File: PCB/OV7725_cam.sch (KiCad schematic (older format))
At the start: 0 parts

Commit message: Camera
Camera sensor and lens mount added to schematic sheet, full scheamtic to
follow
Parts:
- added LENS?: OV7725_20mm_Lens, PCB_Footprints:OV07725_20mm_Lense_Mount, symbol OV7725_20mm_Lens
- added U?: OV7725, PCB_Footprints:OV07725-V28A, symbol OV7725
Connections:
- net labels added: +1V35, +1V8, +3.3V, GND
- wire segments 0 -> 1
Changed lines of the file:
@@
 Comment4 ""
 $EndDescr
+$Comp
+L OV7725 U?
+U 1 1 5882D650
+P 4825 3375
+F 0 "U?" H 4475 4475 60  0000 C CNN
+F 1 "OV7725" H 4575 2675 60  0000 C CNN
+F 2 "PCB_Footprints:OV07725-V28A" H 4875 4575 60  0001 C CNN
+F 3 "https://cdn.shopify.com/s/files/1/0803/9211/files/OV7725.pdf?3787874186050138641" H 4975 4675 60  0001 C CNN
+F 4 "$4.379 @ 36" H 5075 4775 60  0001 C CNN "Cost"
+F 5 "8 Jan 2017" H 5175 4875 60  0001 C CNN "Date Created"
+F 6 "8 Jan 2017" H 5275 4975 60  0001 C CNN "Date Modifed"
+F 7 "Adam Vadala-Roth" H 5375 5075 60  0001 C CNN "Designer"
+F 8 "2.70mm" H 5475 5175 60  0001 C CNN "Height"
+F 9 "Yes" H 5575 5275 60  0001 C CNN "RHoS?"
+F 10 "OmniVision Technologies Inc" H 5675 5375 60  0001 C CNN "MFR"
+F 11 "OV07725-V28A" H 5775 5475 60  0001 C CNN "MFR#"
+F 12 "SMT/SMD" H 5875 5575 60  0001 C CNN "Mounting"
+F 13 "2" H 5975 5675 60  0001 C CNN "Pin Count#"
+F 14 "Active" H 6075 5775 60  0001 C CNN "Status"
+F 15 "N/A" H 6175 5875 60  0001 C CNN "Tolerance"
+F 16 "IC IMAGE SENSOR VGA 28-CSP2" H 6275 5975 60  0001 C CNN "Type"
+F 17 "3.3V" H 6375 6075 60  0001 C CNN "Voltage"
+F 18 "N/A" H 6925 6075 60  0001 C CNN "Wattage"
+F 19 "N/A" H 6525 6375 60  0001 C CNN "Componen-Value"
+F 20 "CMOS Image Sensor 640H x 480V 6µm x 6µm Module" H 7125 6275 60  0001 C CNN "Description"
+	1    4825 3375
+	1    0    0    -1
+$EndComp
+$Comp
+L OV7725_20mm_Lens LENS?
+U 1 1 5882D747
+P 4800 6700
+F 0 "LENS?" H 5378 6778 60  0000 L CNN
+F 1 "OV7725_20mm_Lens" H 5378 6672 60  0000 L CNN
+F 2 "PCB_Footprints:OV07725_20mm_Lense_Mount" H 4850 7900 60  0001 C CNN
+F 3 "https://cdn.shopify.com/s/files/1/0803/9211/files/OV7725.pdf?3787874186050138641" H 4950 8000 60  0001 C CNN
+F 4 "$4.379 @ 36" H 5050 8100 60  0001 C CNN "Cost"
+F 5 "8 Jan 2017" H 5150 8200 60  0001 C CNN "Date Created"
+F 6 "8 Jan 2017" H 5250 8300 60  0001 C CNN "Date Modifed"
+F 7 "Adam Vadala-Roth" H 5350 8400 60  0001 C CNN "Designer"
+F 8 "2.70mm" H 5450 8500 60  0001 C CNN "Height"
+F 9 "Yes" H 5550 8600 60  0001 C CNN "RHoS?"
+F 10 "OmniVision Technologies Inc" H 5650 8700 60  0001 C CNN "MFR"
+F 11 "OV07725-V28A" H 5750 8800 60  0001 C CNN "MFR#"
+F 12 "SMT/SMD" H 5850 8900 60  0001 C CNN "Mounting"
+F 13 "2" H 5950 9000 60  0001 C CNN "Pin Count#"
+F 14 "Active" H 6050 9100 60  0001 C CNN "Status"
+F 15 "N/A" H 6150 9200 60  0001 C CNN "Tolerance"
+F 16 "IC IMAGE SENSOR VGA 28-CSP2" H 6250 9300 60  0001 C CNN "Type"
+F 17 "3.3V" H 6350 9400 60  0001 C CNN "Voltage"
+F 18 "N/A" H 6900 9400 60  0001 C CNN "Wattage"
+F 19 "N/A" H 6500 9700 60  0001 C CNN "Componen-Value"
+F 20 "CMOS Image Sensor 640H x 480V 6µm x 6µm Module" H 7100 9600 60  0001 C CNN "Description"
+	1    4800 6700
+	1    0    0    -1
+$EndComp
+Wire Wire Line
+	4225 3775 4225 3975
+Connection ~ 4225 3875
+$Comp
+L GND #PWR?
+U 1 1 5882E070
+P 4225 3975
+F 0 "#PWR?" H 4225 3725 50  0001 C CNN
+F 1 "GND" H 4230 3802 50  0000 C CNN
+F 2 "" H 4225 3975 50  0000 C CNN
+F 3 "" H 4225 3975 50  0000 C CNN
+	1    4225 3975
+	1    0    0    -1
+$EndComp
+$Comp
+L +3.3V #PWR?
+U 1 1 5882E088
+P 5375 4525
+F 0 "#PWR?" H 5375 4375 50  0001 C CNN
+F 1 "+3.3V" H 5390 4698 50  0000 C CNN
+F 2 "" H 5375 4525 50  0000 C CNN
+F 3 "" H 5375 4525 50  0000 C CNN
+	1    5375 4525
+	1    0    0    -1
+$EndComp
+$Comp
+L +1V8 #PWR?
+U 1 1 5882E0A0
+P 5700 4425
+F 0 "#PWR?" H 5700 4275 50  0001 C CNN
+F 1 "+1V8" H 5715 4598 50  0000 C CNN
+F 2 "" H 5700 4425 50  0000 C CNN
+F 3 "" H 5700 4425 50  0000 C CNN
+	1    5700 4425
+	1    0    0    -1
+$EndComp
+$Comp
+L +1V35 #PWR?
+U 1 1 5882E0B8
+P 6025 3650
+F 0 "#PWR?" H 6025 3500 50  0001 C CNN
+F 1 "+1V35" H 6040 3823 50  0000 C CNN
+F 2 "" H 6025 3650 50  0000 C CNN
+F 3 "" H 6025 3650 50  0000 C CNN
+	1    6025 3650
+	1    0    0    -1
+$EndComp
 $EndSCHEMATC

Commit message: OV07725
Cam schematic drawn, no anotation since I do that at the very end of
scheamtic capture, Next off is the memory and the Zync itself.
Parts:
- removed U?: OV7725, PCB_Footprints:OV07725-V28A, symbol OV7725
- added C? (x6): CL05B104JP5NNNC, PCB_Footprints:C0402, symbol CL05B104JP5NNNC
- added C? (x2): CL21A226KQQNNNE, PCB_Footprints:C0805, symbol CL21A226KQQNNNE
- added FB?: BLM15HG601SN1D, PCB_Footprints:BLM15HG601SN1D, symbol BLM15HG601SN1D
- added R?: RC1005F103CS, PCB_Footprints:R0402, symbol RC1005F103CS
- added R? (x2): RC1005F472CS, PCB_Footprints:R0402, symbol RC1005F472CS
- added R? (x18): ERA-2AEB510X, PCB_Footprints:R0402, symbol ERA-2AEB510X
- added U?: OV07725-V28A, PCB_Footprints:OV07725-V28A, symbol OV07725-V28A
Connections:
- net labels added: CAM_DATA, CAM_HREF, CAM_PCLK, CAM_PWDN, CAM_RST, CAM_SCL, CAM_SDA, CAM_VSYNC, CAM_XCLK, VDDA
- net labels removed: +1V35
- wire segments 1 -> 71
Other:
- note added: "Analog Voltage Supply Bypass Capacitors"
- note added: "Core Voltage Supply Bypass Capacitors"
- note added: "Digital Voltage Supply Bypass Capacitors"
- note added: "Lense and Mounting Assembly"
- note added: "OV0775 CMOS Image Sensor"
- moved on the sheet: LENS?

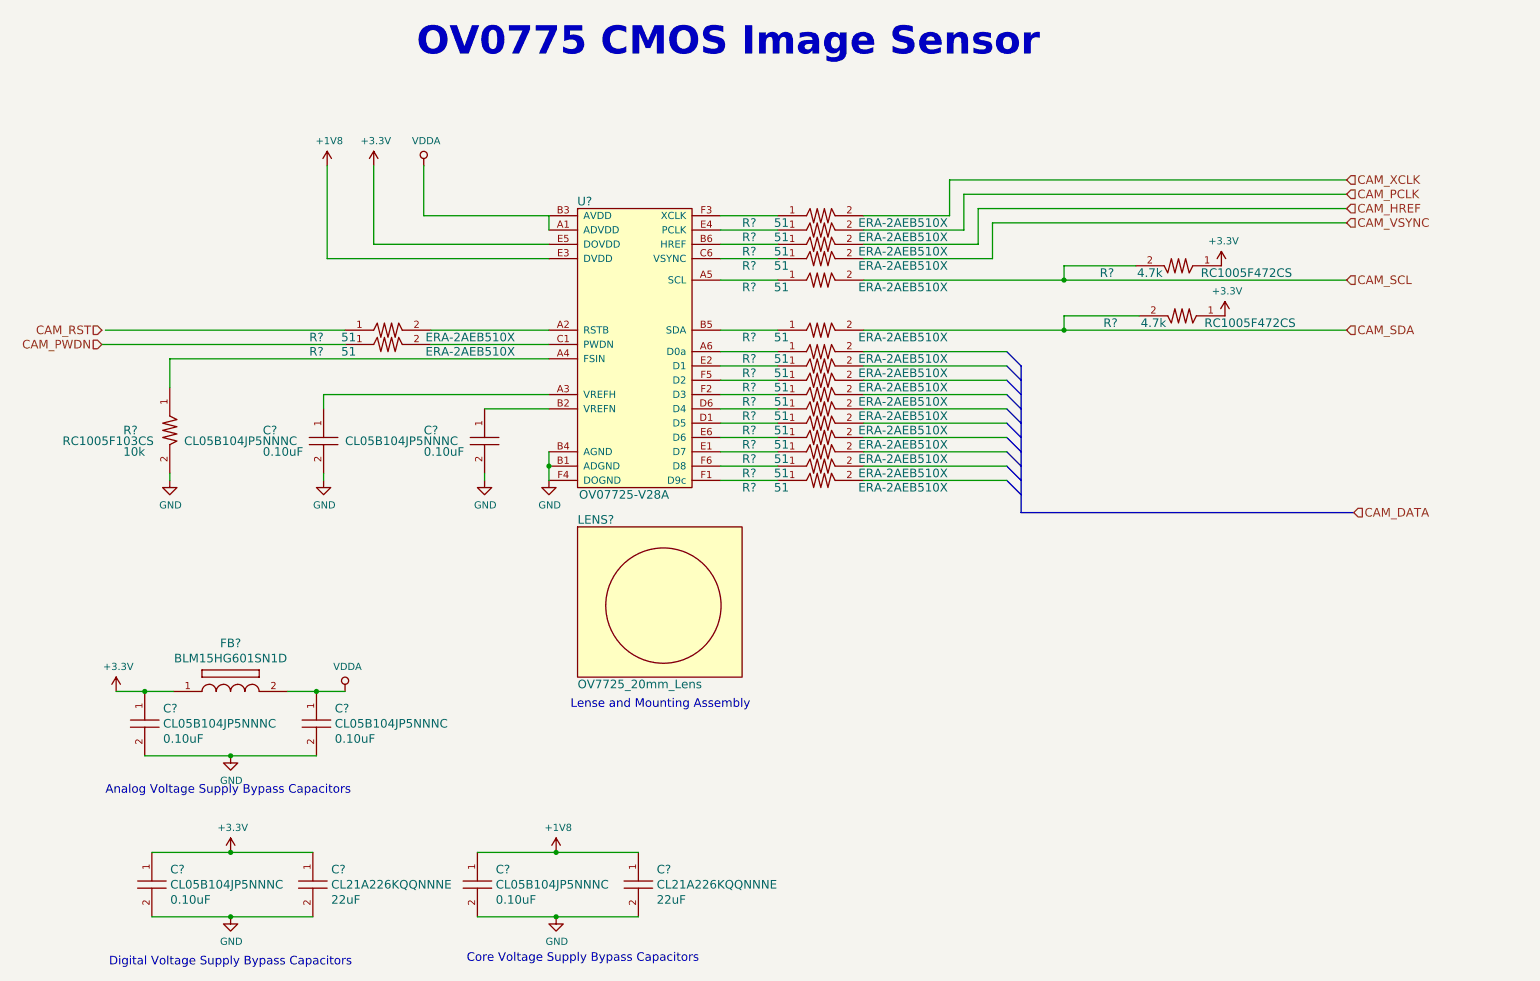
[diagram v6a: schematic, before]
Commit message: Cam / PMIC
Camera data bus entry relabled, PMIC started.
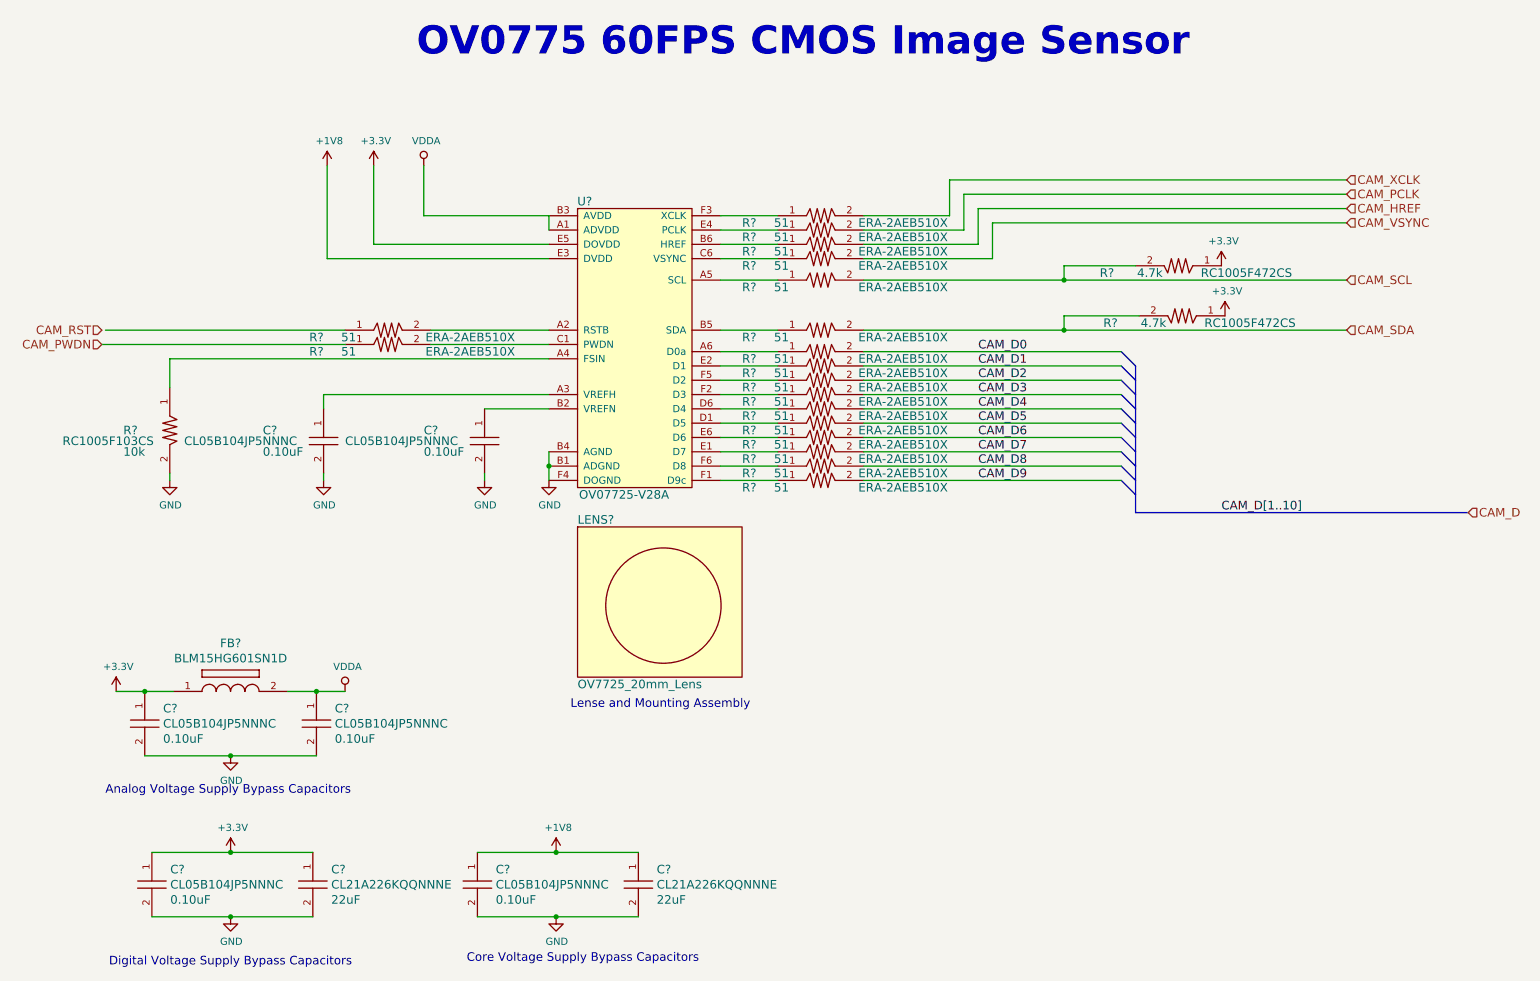
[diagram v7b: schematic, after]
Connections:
- net labels added: CAM_D, CAM_D0, CAM_D1, CAM_D2, CAM_D3, CAM_D4, CAM_D5, CAM_D6, CAM_D7, CAM_D8, CAM_D9, CAM_D[1..10]
- net labels removed: CAM_DATA
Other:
- note added: "OV0775 60FPS CMOS Image Sensor"
- note removed: "OV0775 CMOS Image Sensor"
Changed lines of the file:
@@
 $EndComp
 Wire Wire Line
-	6425 3075 7425 3075
-Wire Wire Line
-	6425 3175 7425 3175
-Wire Wire Line
-	6425 3275 7425 3275
-Wire Wire Line
-	6425 3375 7425 3375
-Wire Wire Line
-	6425 3475 7425 3475
-Wire Wire Line
-	6425 3575 7425 3575
-Wire Wire Line
-	6425 3675 7425 3675
-Wire Wire Line
-	6425 3775 7425 3775
-Wire Wire Line
-	6425 3875 7425 3875
-Wire Wire Line
-	6425 3975 7425 3975
-Entry Bus Bus
-	7425 3075 7525 3175
-Entry Bus Bus
-	7425 3175 7525 3275
-Entry Bus Bus
-	7425 3275 7525 3375
-Entry Bus Bus
-	7425 3375 7525 3475
-Entry Bus Bus
-	7425 3475 7525 3575
-Entry Bus Bus
-	7425 3575 7525 3675
-Entry Bus Bus
-	7425 3675 7525 3775
-Entry Bus Bus
-	7425 3775 7525 3875
-Entry Bus Bus
-	7425 3875 7525 3975
-Entry Bus Bus
-	7425 3975 7525 4075
+	6425 3075 8225 3075
+Wire Wire Line
+	6425 3175 8225 3175
+Wire Wire Line
+	6425 3275 8225 3275
+Wire Wire Line
+	6425 3375 8225 3375
+Wire Wire Line
+	6425 3475 8225 3475
+Wire Wire Line
+	6425 3575 8225 3575
+Wire Wire Line
+	6425 3675 8225 3675
+Wire Wire Line
+	6425 3775 8225 3775
+Wire Wire Line
+	6425 3875 8225 3875
+Wire Wire Line
+	6425 3975 8225 3975
+Entry Bus Bus
+	8225 3075 8325 3175
+Entry Bus Bus
+	8225 3175 8325 3275
+Entry Bus Bus
+	8225 3275 8325 3375
+Entry Bus Bus
+	8225 3375 8325 3475
+Entry Bus Bus
+	8225 3475 8325 3575
+Entry Bus Bus
+	8225 3575 8325 3675
+Entry Bus Bus
+	8225 3675 8325 3775
+Entry Bus Bus
+	8225 3775 8325 3875
+Entry Bus Bus
+	8225 3875 8325 3975
+Entry Bus Bus
+	8225 3975 8325 4075
 Wire Bus Line
-	7525 3175 7525 4200
+	8325 3175 8325 4200
 Wire Bus Line
-	7525 4200 9850 4200
-Text HLabel 9850 4200 2    60   Input ~ 0
-CAM_DATA
+	8325 4200 10650 4200
+Text HLabel 10650 4200 2    60   Input ~ 0
+CAM_D
 Wire Wire Line
 	7325 2425 7325 2175
@@
 CAM_PCLK
 Text Notes 3300 1025 0    197  ~ 39
-OV0775 CMOS Image Sensor
+OV0775 60FPS CMOS Image Sensor
 Text HLabel 9800 2075 2    60   Input ~ 0
 CAM_HREF
@@
 Wire Wire Line
 	1125 2925 2800 2925
+Text Label 8925 4200 0    60   ~ 0
+CAM_D[1..10]
+Text Label 7225 3075 0    60   ~ 0
+CAM_D0
+Text Label 7225 3175 0    60   ~ 0
+CAM_D1
+Text Label 7225 3275 0    60   ~ 0
+CAM_D2
+Text Label 7225 3375 0    60   ~ 0
+CAM_D3
+Text Label 7225 3475 0    60   ~ 0
+CAM_D4
+Text Label 7225 3575 0    60   ~ 0
+CAM_D5
+Text Label 7225 3675 0    60   ~ 0
+CAM_D6
+Text Label 7225 3775 0    60   ~ 0
+CAM_D7
+Text Label 7225 3875 0    60   ~ 0
+CAM_D8
+Text Label 7225 3975 0    60   ~ 0
+CAM_D9
 $EndSCHEMATC
